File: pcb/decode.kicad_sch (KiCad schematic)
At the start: 20 parts, among them Q165 2N7002a, Q166 2N7002a, Q167 2N7002a, Q168 2N7002a, Q169 2N7002a, Q170 2N7002a, Q171 2N7002a, Q172 2N7002a, Q173 2N7002a, Q174 2N7002a, Q175 2N7002a, Q176 2N7002a, Q177 2N7002a, Q178 2N7002a

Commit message: Pi programmer.
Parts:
- renumbered Q165 to Q83, Q166 to Q84, Q167 to Q85, Q168 to Q86, Q169 to Q87, Q170 to Q88, Q171 to Q89, Q172 to Q90, Q173 to Q91, Q174 to Q92, Q175 to Q93, Q176 to Q94, Q177 to Q95, Q178 to Q96, R70 to R35, R71 to R36, R72 to R37, R73 to R38, R74 to R39, R75 to R40
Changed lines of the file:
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@@
   (symbol (lib_id "power:VCC") (at 71.12 38.1 0) (unit 1)
     (in_bom yes) (on_board yes)
-    (property "Reference" "#PWR0162" (id 0) (at 71.12 41.91 0)
+    (property "Reference" "#PWR097" (id 0) (at 71.12 41.91 0)
       (effects (font (size 1.27 1.27)) hide)
     )
@@
   (symbol (lib_id "power:VCC") (at 95.25 38.1 0) (unit 1)
     (in_bom yes) (on_board yes)
-    (property "Reference" "#PWR0163" (id 0) (at 95.25 41.91 0)
+    (property "Reference" "#PWR098" (id 0) (at 95.25 41.91 0)
       (effects (font (size 1.27 1.27)) hide)
     )
@@
   (symbol (lib_id "power:VCC") (at 119.38 38.1 0) (unit 1)
     (in_bom yes) (on_board yes)
-    (property "Reference" "#PWR0164" (id 0) (at 119.38 41.91 0)
+    (property "Reference" "#PWR099" (id 0) (at 119.38 41.91 0)
       (effects (font (size 1.27 1.27)) hide)
     )
@@
   (symbol (lib_id "power:VCC") (at 143.51 38.1 0) (unit 1)
     (in_bom yes) (on_board yes)
-    (property "Reference" "#PWR0165" (id 0) (at 143.51 41.91 0)
+    (property "Reference" "#PWR0100" (id 0) (at 143.51 41.91 0)
       (effects (font (size 1.27 1.27)) hide)
     )
@@
   (symbol (lib_id "power:VCC") (at 154.94 80.01 0) (unit 1)
     (in_bom yes) (on_board yes)
-    (property "Reference" "#PWR0167" (id 0) (at 154.94 83.82 0)
+    (property "Reference" "#PWR0102" (id 0) (at 154.94 83.82 0)
       (effects (font (size 1.27 1.27)) hide)
     )
@@
   (symbol (lib_id "power:VCC") (at 171.45 71.12 0) (unit 1)
     (in_bom yes) (on_board yes)
-    (property "Reference" "#PWR0166" (id 0) (at 171.45 74.93 0)
+    (property "Reference" "#PWR0101" (id 0) (at 171.45 74.93 0)
       (effects (font (size 1.27 1.27)) hide)
     )
@@
   (symbol (lib_id "power:GND") (at 71.12 115.57 0) (unit 1)
     (in_bom yes) (on_board yes)
-    (property "Reference" "#PWR0169" (id 0) (at 71.12 121.92 0)
+    (property "Reference" "#PWR0104" (id 0) (at 71.12 121.92 0)
       (effects (font (size 1.27 1.27)) hide)
     )
@@
   (symbol (lib_id "power:GND") (at 147.32 121.92 0) (unit 1)
     (in_bom yes) (on_board yes)
-    (property "Reference" "#PWR0170" (id 0) (at 147.32 128.27 0)
+    (property "Reference" "#PWR0105" (id 0) (at 147.32 128.27 0)
       (effects (font (size 1.27 1.27)) hide)
     )
@@
   (symbol (lib_id "power:GND") (at 171.45 111.76 0) (unit 1)
     (in_bom yes) (on_board yes)
-    (property "Reference" "#PWR0168" (id 0) (at 171.45 118.11 0)
+    (property "Reference" "#PWR0103" (id 0) (at 171.45 118.11 0)
       (effects (font (size 1.27 1.27)) hide)
     )
@@
   (symbol (lib_id "Device:R") (at 71.12 41.91 0) (unit 1)
     (in_bom yes) (on_board yes)
-    (property "Reference" "R70" (id 0) (at 72.898 40.7416 0)
+    (property "Reference" "R35" (id 0) (at 72.898 40.7416 0)
       (effects (font (size 1.27 1.27)) (justify left))
     )
@@
   (symbol (lib_id "Device:R") (at 95.25 41.91 0) (unit 1)
     (in_bom yes) (on_board yes)
-    (property "Reference" "R71" (id 0) (at 97.028 40.7416 0)
+    (property "Reference" "R36" (id 0) (at 97.028 40.7416 0)
       (effects (font (size 1.27 1.27)) (justify left))
     )
@@
   (symbol (lib_id "Device:R") (at 119.38 41.91 0) (unit 1)
     (in_bom yes) (on_board yes)
-    (property "Reference" "R72" (id 0) (at 121.158 40.7416 0)
+    (property "Reference" "R37" (id 0) (at 121.158 40.7416 0)
       (effects (font (size 1.27 1.27)) (justify left))
     )
@@
   (symbol (lib_id "Device:R") (at 143.51 41.91 0) (unit 1)
     (in_bom yes) (on_board yes)
-    (property "Reference" "R73" (id 0) (at 145.288 40.7416 0)
+    (property "Reference" "R38" (id 0) (at 145.288 40.7416 0)
       (effects (font (size 1.27 1.27)) (justify left))
     )
@@
   (symbol (lib_id "Device:R") (at 154.94 83.82 0) (unit 1)
     (in_bom yes) (on_board yes)
-    (property "Reference" "R75" (id 0) (at 156.718 82.6516 0)
+    (property "Reference" "R40" (id 0) (at 156.718 82.6516 0)
       (effects (font (size 1.27 1.27)) (justify left))
     )
@@
   (symbol (lib_id "Device:R") (at 171.45 74.93 0) (unit 1)
     (in_bom yes) (on_board yes)
-    (property "Reference" "R74" (id 0) (at 173.228 73.7616 0)
+    (property "Reference" "R39" (id 0) (at 173.228 73.7616 0)
       (effects (font (size 1.27 1.27)) (justify left))
     )
@@
   (symbol (lib_id "Transistor_FET:2N7002") (at 68.58 68.58 0) (unit 1)
     (in_bom yes) (on_board yes)
-    (property "Reference" "Q167" (id 0) (at 73.8124 67.4116 0)
+    (property "Reference" "Q85" (id 0) (at 73.8124 67.4116 0)
       (effects (font (size 1.27 1.27)) (justify left))
     )
@@
   (symbol (lib_id "Transistor_FET:2N7002") (at 68.58 85.09 0) (unit 1)
     (in_bom yes) (on_board yes)
-    (property "Reference" "Q172" (id 0) (at 73.8124 83.9216 0)
+    (property "Reference" "Q90" (id 0) (at 73.8124 83.9216 0)
       (effects (font (size 1.27 1.27)) (justify left))
     )
@@
   (symbol (lib_id "Transistor_FET:2N7002") (at 68.58 100.33 0) (unit 1)
     (in_bom yes) (on_board yes)
-    (property "Reference" "Q174" (id 0) (at 73.8124 99.1616 0)
+    (property "Reference" "Q92" (id 0) (at 73.8124 99.1616 0)
       (effects (font (size 1.27 1.27)) (justify left))
     )
@@
   (symbol (lib_id "Transistor_FET:2N7002") (at 68.58 110.49 0) (unit 1)
     (in_bom yes) (on_board yes)
-    (property "Reference" "Q177" (id 0) (at 73.8124 109.3216 0)
+    (property "Reference" "Q95" (id 0) (at 73.8124 109.3216 0)
       (effects (font (size 1.27 1.27)) (justify left))
     )
@@
   (symbol (lib_id "Transistor_FET:2N7002") (at 92.71 58.42 0) (unit 1)
     (in_bom yes) (on_board yes)
-    (property "Reference" "Q165" (id 0) (at 97.9424 57.2516 0)
+    (property "Reference" "Q83" (id 0) (at 97.9424 57.2516 0)
       (effects (font (size 1.27 1.27)) (justify left))
     )
@@
   (symbol (lib_id "Transistor_FET:2N7002") (at 92.71 68.58 0) (unit 1)
     (in_bom yes) (on_board yes)
-    (property "Reference" "Q168" (id 0) (at 97.9424 67.4116 0)
+    (property "Reference" "Q86" (id 0) (at 97.9424 67.4116 0)
       (effects (font (size 1.27 1.27)) (justify left))
     )
@@
   (symbol (lib_id "Transistor_FET:2N7002") (at 116.84 58.42 0) (unit 1)
     (in_bom yes) (on_board yes)
-    (property "Reference" "Q166" (id 0) (at 122.0724 57.2516 0)
+    (property "Reference" "Q84" (id 0) (at 122.0724 57.2516 0)
       (effects (font (size 1.27 1.27)) (justify left))
     )
@@
   (symbol (lib_id "Transistor_FET:2N7002") (at 116.84 68.58 0) (unit 1)
     (in_bom yes) (on_board yes)
-    (property "Reference" "Q169" (id 0) (at 122.0724 67.4116 0)
+    (property "Reference" "Q87" (id 0) (at 122.0724 67.4116 0)
       (effects (font (size 1.27 1.27)) (justify left))
     )
@@
   (symbol (lib_id "Transistor_FET:2N7002") (at 116.84 82.55 0) (unit 1)
     (in_bom yes) (on_board yes)
-    (property "Reference" "Q171" (id 0) (at 122.0724 81.3816 0)
+    (property "Reference" "Q89" (id 0) (at 122.0724 81.3816 0)
       (effects (font (size 1.27 1.27)) (justify left))
     )
@@
   (symbol (lib_id "Transistor_FET:2N7002") (at 140.97 68.58 0) (unit 1)
     (in_bom yes) (on_board yes)
-    (property "Reference" "Q170" (id 0) (at 146.2024 67.4116 0)
+    (property "Reference" "Q88" (id 0) (at 146.2024 67.4116 0)
       (effects (font (size 1.27 1.27)) (justify left))
     )
@@
   (symbol (lib_id "Transistor_FET:2N7002") (at 144.78 106.68 0) (unit 1)
     (in_bom yes) (on_board yes)
-    (property "Reference" "Q175" (id 0) (at 150.0124 105.5116 0)
+    (property "Reference" "Q93" (id 0) (at 150.0124 105.5116 0)
       (effects (font (size 1.27 1.27)) (justify left))
     )
@@
   (symbol (lib_id "Transistor_FET:2N7002") (at 144.78 116.84 0) (unit 1)
     (in_bom yes) (on_board yes)
-    (property "Reference" "Q178" (id 0) (at 150.0124 115.6716 0)
+    (property "Reference" "Q96" (id 0) (at 150.0124 115.6716 0)
       (effects (font (size 1.27 1.27)) (justify left))
     )
@@
   (symbol (lib_id "Transistor_FET:2N7002") (at 168.91 92.71 0) (unit 1)
     (in_bom yes) (on_board yes)
-    (property "Reference" "Q173" (id 0) (at 174.1424 91.5416 0)
+    (property "Reference" "Q91" (id 0) (at 174.1424 91.5416 0)
       (effects (font (size 1.27 1.27)) (justify left))
     )
@@
   (symbol (lib_id "Transistor_FET:2N7002") (at 168.91 106.68 0) (unit 1)
     (in_bom yes) (on_board yes)
-    (property "Reference" "Q176" (id 0) (at 174.1424 105.5116 0)
-      (effects (font (size 1.27 1.27)) (justify left))
-    )
+    (property "Reference" "Q94" (id 0) (at 174.1424 105.5116 0)
+      (effects (font (size 1.27 1.27)) (justify left))
+    )

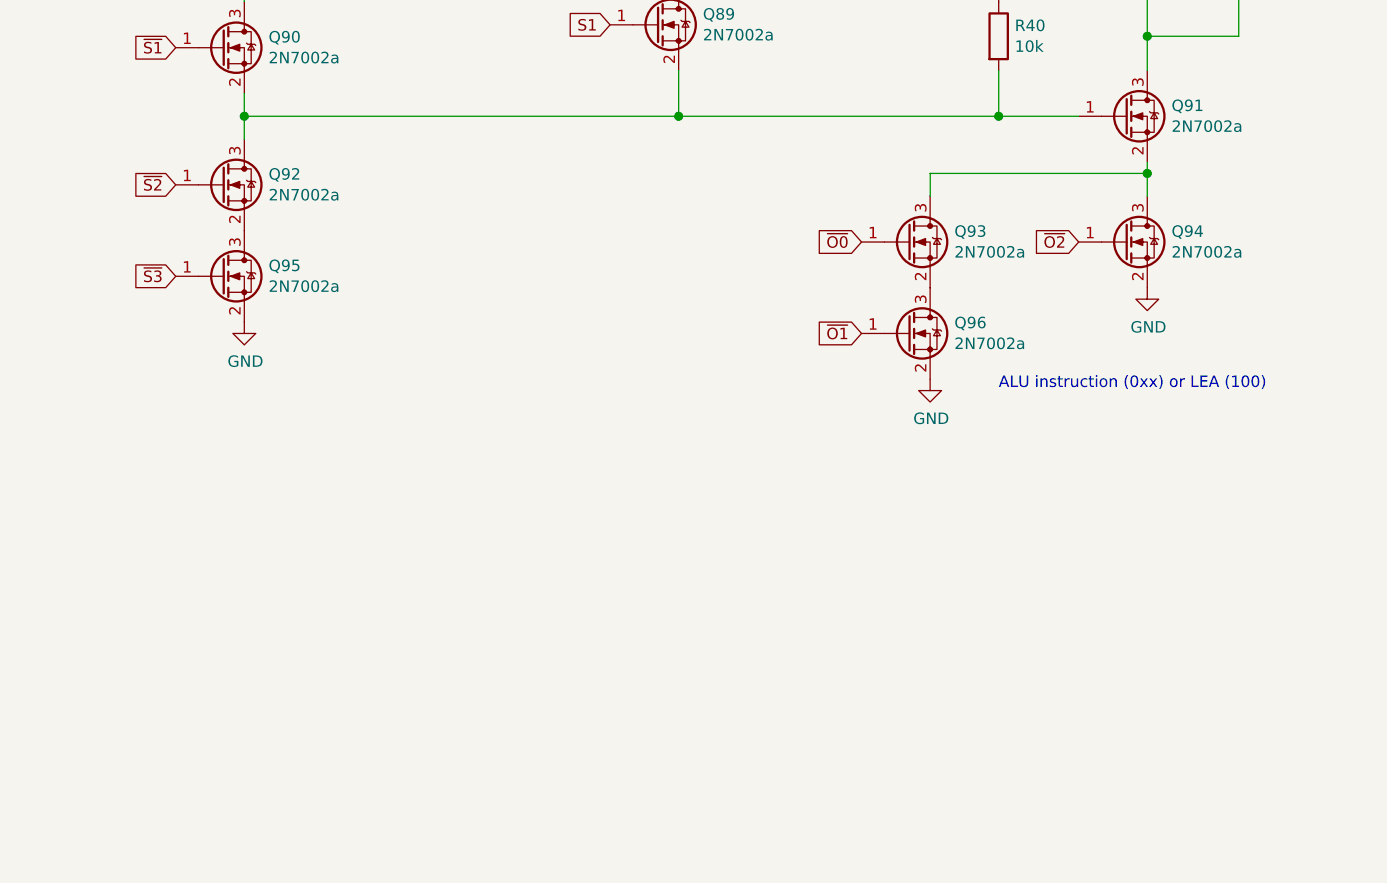
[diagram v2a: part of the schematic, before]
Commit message: Skip ALU state for jfc/jmp/sta.
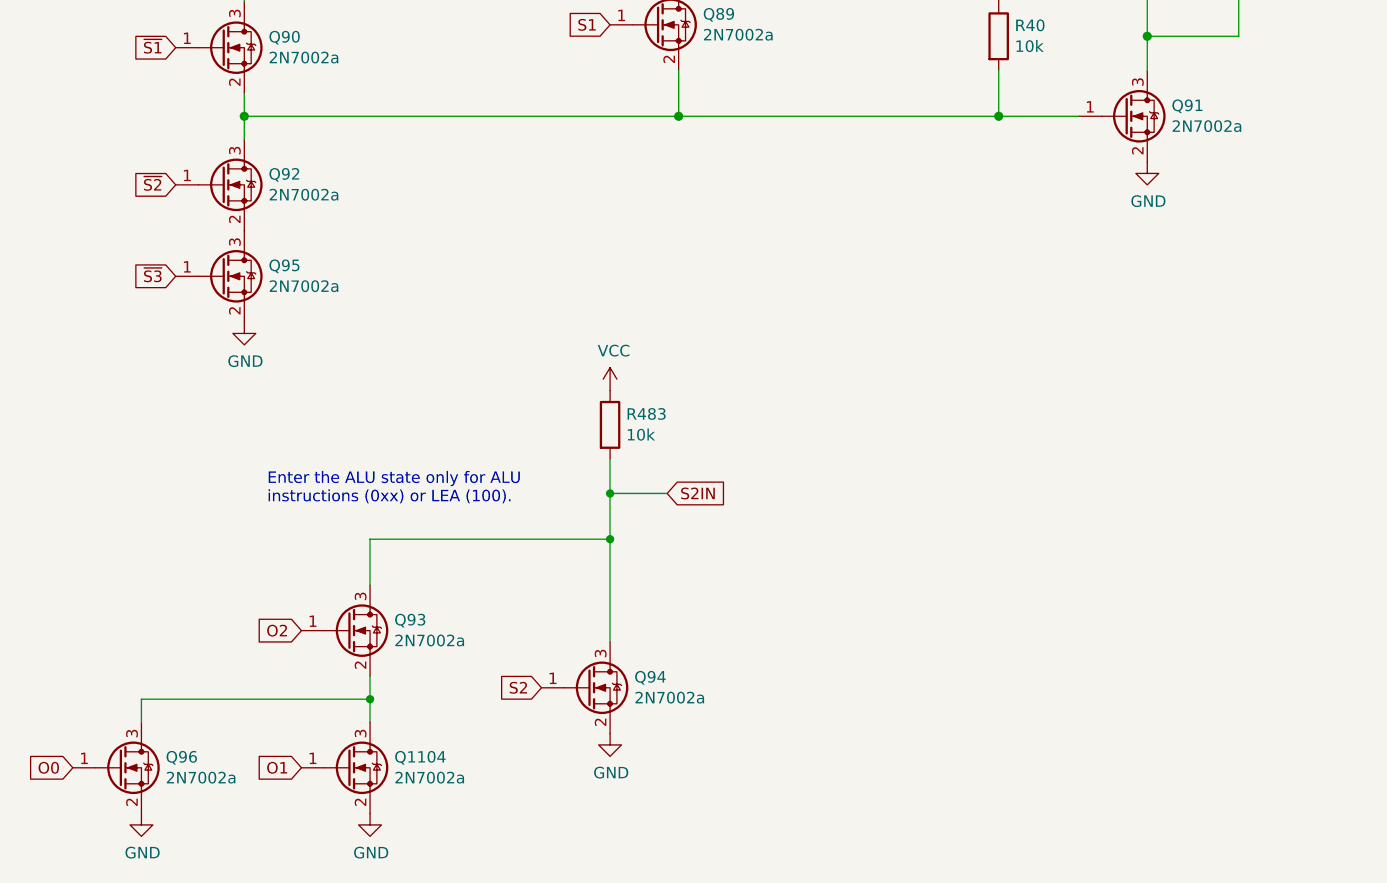
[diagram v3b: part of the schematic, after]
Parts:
- added Q1104: 2N7002a, Package_TO_SOT_SMD:SOT-23, symbol Transistor_FET:2N7002
- added R483: 10k, Resistor_SMD:R_0805_2012Metric, symbol Device:R
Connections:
- net GND: now also Q91.2 (S), Q1104.2 (S)
- net VCC: now also R483.1
- net ~O2: no longer Q94.1 (G)
- net S2IN: now reaches Q93.3 (D), Q94.3 (D)
- net S2IN: now also R483.2; no longer Q91.2 (S)
- net at Q93.2 (S), Q96.3 (D): now also Q1104.3 (D)
- net ~O0 renamed O2
- net ~O1 renamed O0
- new net O1: Q1104.1 (G)
- new net S2: Q94.1 (G)
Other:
- note added: "Enter the ALU state only for ALU instructions (0xx) or LEA (100)."
- note removed: "ALU instruction (0xx) or LEA (100)"

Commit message: Some fixes.
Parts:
- removed R39: 10k, Resistor_SMD:R_0805_2012Metric, symbol Device:R
- added R40: 1k, Resistor_SMD:R_0805_2012Metric, symbol Device:R
- R35: value 10k -> 1k; LCSC C17414 -> C17513
- renumbered Q83 to Q82, Q84 to Q83, Q85 to Q84, Q86 to Q85, Q87 to Q86, Q88 to Q87, Q89 to Q88, Q90 to Q89, Q91 to Q90, Q92 to Q91, Q95 to Q92, Q96 to Q95, Q1104 to Q96, R40 to R41, R483 to R42
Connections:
- net VCC: now also R40.1
- net ~STATE_ALU: now also R40.2
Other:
- note added: "Fanout to 17 gates. From SC: 2.8+0.6 = 3.4us"
- note added: "Fanout to 19 gates. From SC: 2.8+0.7=3.5us."
- note added: "Fanout to 2 gates"
- note added: "Fanout to 6 gates. From SC: 2.8+2.1=4.9us."
- note added: "SC goes through 4 flip flops (S0..S3). Each flip flop has 2 levels of logic and 2 gates for each level. Assuming Vth=2.5, Cg=50pF, and R=10k we arrive at: t = 2.8us The fanout of the state flip flops affect the time for the state to be stable. Max delay is under 5us."
- moved on the sheet: Q82, Q83, Q84, Q85, Q86, Q87, Q88, Q89, Q90, Q91, Q92, Q93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

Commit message: Faster.
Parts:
- removed R36, R38: 10k, Resistor_SMD:R_0805_2012Metric, symbol Device:R
- added R37, R485, R486, R487, R488: 10k, Resistor_SMD:R_0805_2012Metric, symbol Device:R
- renumbered R37 to R36, R40 to R38, R41 to R39, R42 to R40
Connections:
- net ~STATE_DEREF is gone; now on net ~STATE_LOAD: Q82.3 (D)
- net VCC: now also R37.1, R485.1, R486.1, R487.1, R488.1
- net ~S0: now also R485.2
- net ~S1: now also R486.2
- net ~S2: now also R487.2
- net ~S3: now also R488.2
- net ~STATE_EXEC: now also R37.2
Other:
- note added: "Extra pull-ups for the state outputs used to clock the next state. This brings the max delay of the state bits from 8.7us to 6.4us."
- note added: "Fanout to 17 gates (0.6us)"
- note added: "Fanout to 19 gates (0.7us)"
- note added: "Fanout to 2 gates (0.7us)"
- note added: "Fanout to 6 gates (2.1us)"
- note added: "Max delay through the decoder is 2.1us. Delay through state bits is 6.4us. Delay from SC to states is 8.5us."
- note added: "SC goes through 4 flip flops (S0..S3). Each flip flop is two levels of logic. The max fanout at the first level is 3. For the second level it is 4 for S0 and 3 for the rest. Assuming Vth=2.5, Cg=50pF, Ra=10k (first level), and Rb=5k (second level) we arrive at 6.4us for all state bits to be stable."
- note added: "~S0~ clocks S1, ~S0~ fanout: 4 ~S1~ clocks S2, ~S1~ fanout: 3 ~S2~ clocks S3, ~S2~ fanout: 3 ~S3~ fanout: 3"
- note removed: "Fanout to 17 gates. From SC: 2.8+0.6 = 3.4us"
- note removed: "Fanout to 19 gates. From SC: 2.8+0.7=3.5us."
- note removed: "Fanout to 2 gates"
- note removed: "Fanout to 6 gates. From SC: 2.8+2.1=4.9us."
- note removed: "SC goes through 4 flip flops (S0..S3). Each flip flop has 2 levels of logic and 2 gates for each level. Assuming Vth=2.5, Cg=50pF, and R=10k we arrive at: t = 2.8us The fanout of the state flip flops affect the time for the state to be stable. Max delay is under 5us."
- moved on the sheet: R36

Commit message: Updates
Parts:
- removed R485, R486, R487, R488: 10k, Resistor_SMD:R_0805_2012Metric, symbol Device:R
- Q82, Q83, Q84, Q85, Q86, Q87, Q88, Q89, Q90, Q91, Q92, Q93, Q94, Q95, Q96: value 2N7002a -> 2N7002; LCSC C8545 -> C181083
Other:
- note added: "Max delay through the decoder is 2.1us. Delay through state bits is 8.7us. Delay from SC to states is 10.3us."
- note added: "SC goes through 4 flip flops (S0..S3). Each flip flop is two levels of logic. The max fanout at the first level is 3. For the second level it is 4 for S0 and 3 for the rest. Assuming Vth=2.5, Cg=50pF, and R=10k, we arrive at 8.7us for all state bits to be stable."
- note removed: "Extra pull-ups for the state outputs used to clock the next state. This brings the max delay of the state bits from 8.7us to 6.4us."
- note removed: "Max delay through the decoder is 2.1us. Delay through state bits is 6.4us. Delay from SC to states is 8.5us."
- note removed: "SC goes through 4 flip flops (S0..S3). Each flip flop is two levels of logic. The max fanout at the first level is 3. For the second level it is 4 for S0 and 3 for the rest. Assuming Vth=2.5, Cg=50pF, Ra=10k (first level), and Rb=5k (second level) we arrive at 6.4us for all state bits to be stable."
